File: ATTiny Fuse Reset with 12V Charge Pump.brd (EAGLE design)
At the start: 68.6 x 53.3 mm, 59 parts, among them IC1 74HC04D, Q1 BSS138, Q2 PMV65XP, Q3 BSS138, Q4 BSS138, Q5 BSS138, Q6 BSS138, Q7 BSS138, Q8 BSS130, SW4 SWITCH_SPDT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

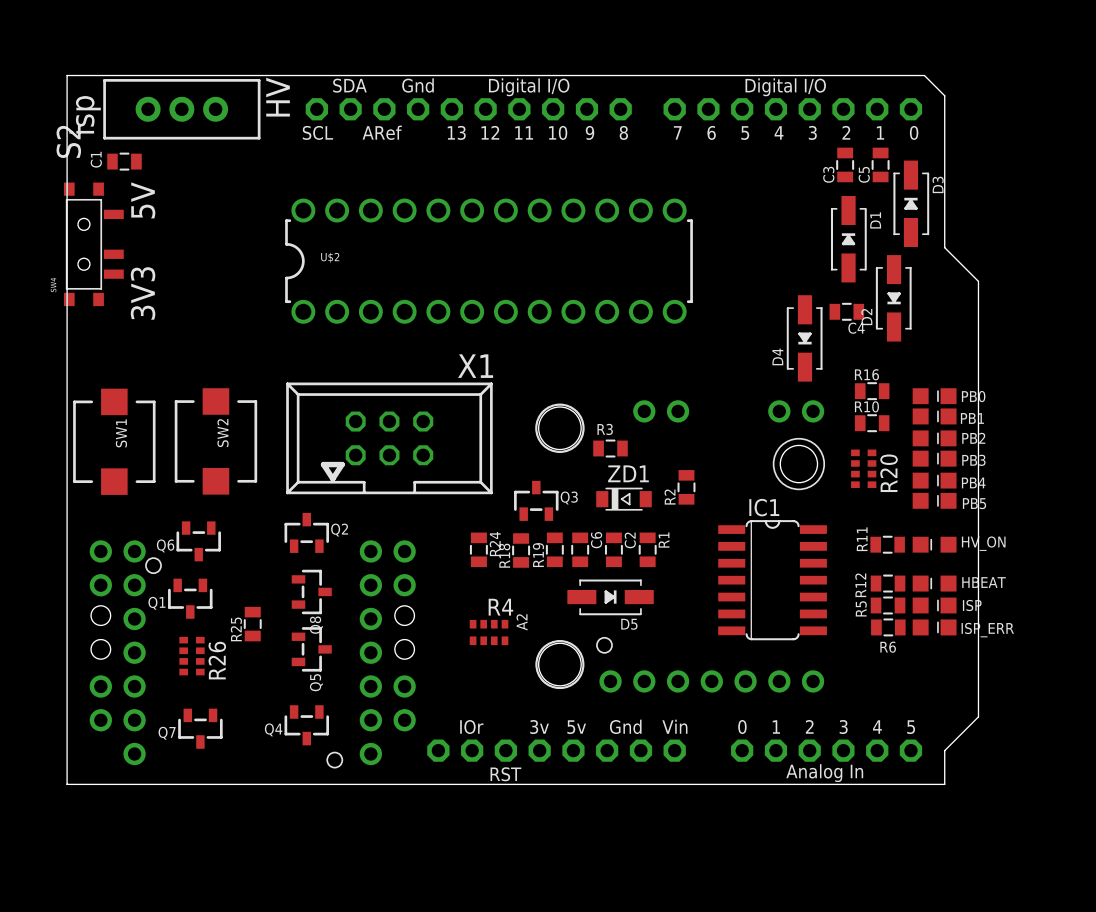
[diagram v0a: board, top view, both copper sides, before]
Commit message: removed pins from silkscreen on arduino device
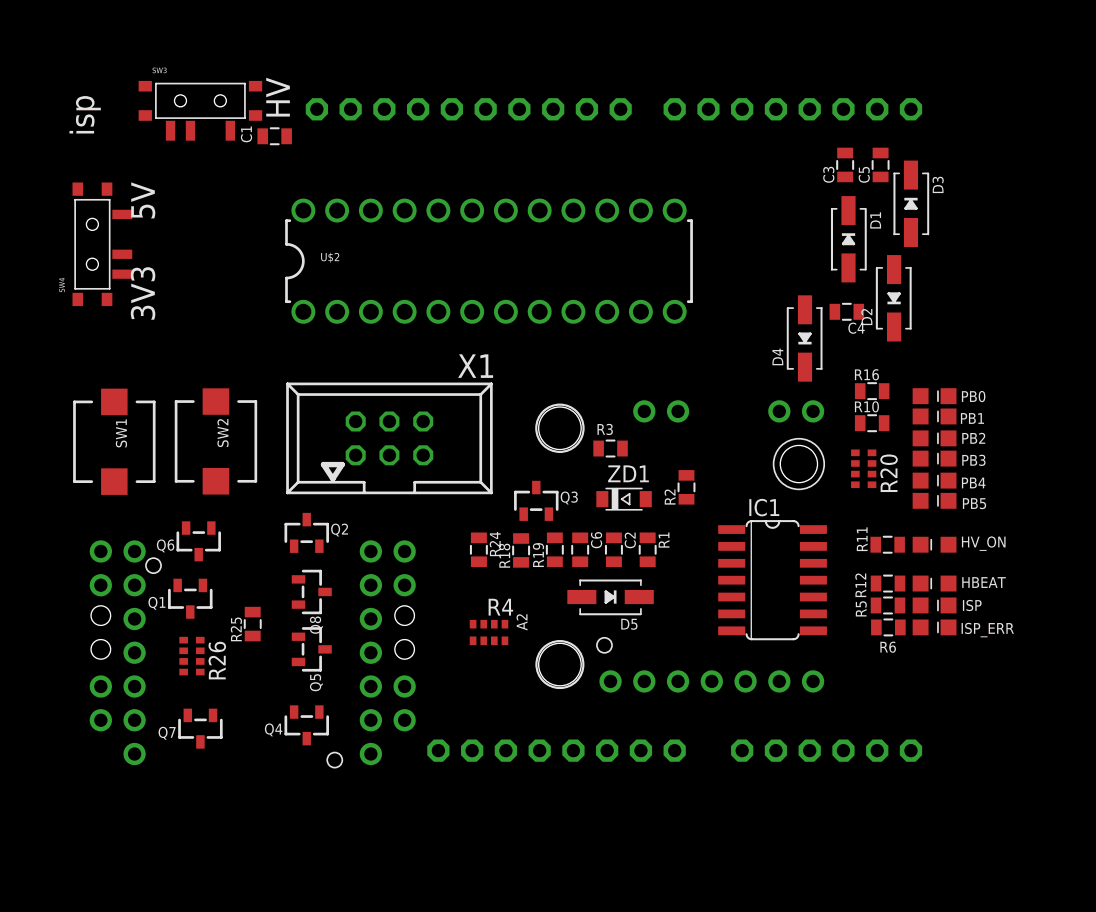
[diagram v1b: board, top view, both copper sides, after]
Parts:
- removed S2: (no value), SparkFun-Electromechanical:SWITCH-SPDT
- added SW3: SWITCH_SPDT, SparkFun-Electromechanical:KPS-1290
- U1: value ARDUINOR3 -> ARDUINOR3-BPLACE; device ATtami:ARDUINO_CLEAN -> ATtami:ARDUINOR3-BPLACE
- moved C1 11.5 mm to (15.6, 48.8)
- moved SW4 0.64 mm to (1.91, 40.6)
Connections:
- net GND: now also SW3.P; no longer S2.2
- net N$14: now also SW3.O; no longer S2.1
- net N$3: now also SW3.S; no longer S2.3
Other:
- board outline removed
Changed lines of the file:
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@@
 <layer number="23" name="tOrigins" color="15" fill="1" visible="yes" active="yes"/>
 <layer number="24" name="bOrigins" color="15" fill="1" visible="yes" active="yes"/>
-<layer number="25" name="tNames" color="7" fill="1" visible="yes" active="yes"/>
+<layer number="25" name="tNames" color="7" fill="1" visible="no" active="yes"/>
 <layer number="26" name="bNames" color="7" fill="1" visible="no" active="yes"/>
 <layer number="27" name="tValues" color="7" fill="1" visible="no" active="yes"/>
@@
 <attribute name="NAME" x="45.7835" y="20.955" size="0.8128" layer="25" rot="R90"/>
 </element>
-<element name="U1" library="ATtami" package="ARDUINO_CLEAN" value="ARDUINOR3" x="0" y="0"/>
+<element name="U1" library="ATtami" package="ARDUINOR3-BPLACE" value="ARDUINOR3-BPLACE" x="0" y="0"/>
 <element name="R11" library="ATtami" package="0805" value="220R" x="61.7474" y="18.034" smashed="yes" rot="R180">
 <attribute name="NAME" x="59.4233" y="19.431" size="0.8128" layer="25" rot="R270"/>
@@
 <attribute name="NAME" x="43.01" y="12.462" size="0.8128" layer="25" ratio="18" rot="R180"/>
 </element>
-<element name="C1" library="ATtami" package="0805" value="10uF" x="4.318" y="46.863" smashed="yes">
-<attribute name="NAME" x="2.6035" y="46.355" size="0.8128" layer="25" rot="R90"/>
-</element>
-<element name="SW4" library="SparkFun-Electromechanical" package="KPS-1290" value="SWITCH_SPDT" x="1.27" y="40.64" rot="R270"/>
+<element name="C1" library="ATtami" package="0805" value="10uF" x="15.621" y="48.768" smashed="yes">
+<attribute name="NAME" x="13.9065" y="48.26" size="0.8128" layer="25" rot="R90"/>
+</element>
+<element name="SW4" library="SparkFun-Electromechanical" package="KPS-1290" value="SWITCH_SPDT" x="1.905" y="40.64" rot="R270"/>
 <element name="ZD1" library="dp_devices" package="SOD-123" value="12V_zener" x="41.91" y="21.463" smashed="yes">
 <attribute name="NAME" x="40.64" y="22.733" size="1.27" layer="25" font="vector" ratio="10"/>
@@
 <element name="JP1" library="SparkFun-Connectors" package="1X02_PP_HOLES_ONLY" value="M02POGO_PIN_HOLES_ONLY" x="25.4" y="10.16" rot="R90"/>
 <element name="JP2" library="SparkFun-Connectors" package="1X02_PP_HOLES_ONLY" value="M02POGO_PIN_HOLES_ONLY" x="2.54" y="10.16" rot="R90"/>
-<element name="S2" library="SparkFun-Electromechanical" package="SWITCH-SPDT" value="" x="8.636" y="50.8" rot="R90">
-<attribute name="PROD_ID" value="SWCH-08261" x="8.636" y="50.8" size="1.778" layer="27" font="vector" ratio="15" rot="R90" display="off"/>
-</element>
 <element name="R4" library="SparkFun-Passives" package="0603-ARV" value="4k7" x="31.75" y="11.43" rot="R180"/>
 <element name="U$2" library="ATTiny Fuse Reset with 12V Charge Pump" package="DIL-24-ZIF" value="ZIFSOCKET-24" x="31.75" y="39.37"/>
+<element name="SW3" library="SparkFun-Electromechanical" package="KPS-1290" value="SWITCH_SPDT" x="10.033" y="51.435" rot="R180"/>
 </elements>
 <signals>
@@
 <contactref element="X1" pad="6"/>
 <contactref element="R25" pad="2"/>
-<contactref element="S2" pad="2"/>
-<contactref element="U1" pad="GND"/>
 <contactref element="U$2" pad="P$16"/>
 <contactref element="U$2" pad="P$18"/>
@@
 <contactref element="U$2" pad="P$17"/>
 <contactref element="U$2" pad="P$4"/>
+<contactref element="SW3" pad="P"/>
+<contactref element="U1" pad="GND"/>
 <wire x1="45.974" y1="28.067" x2="56.134" y2="28.067" width="0" layer="19" extent="1-1"/>
 <wire x1="46.609" y1="21.452" x2="45.974" y2="28.067" width="0" layer="19" extent="1-1"/>
@@
 <wire x1="26.416" y1="50.8" x2="30.48" y2="43.18" width="0" layer="19" extent="1-1"/>
 <wire x1="25.4" y1="7.366" x2="17.415" y2="13.528" width="0" layer="19" extent="1-1"/>
-<wire x1="8.636" y1="50.8" x2="26.416" y2="50.8" width="0" layer="19" extent="1-1"/>
+<wire x1="9.283" y1="49.185" x2="26.416" y2="50.8" width="0" layer="19" extent="1-1"/>
 </signal>
 <signal name="VIN">
@@
 <contactref element="R4" pad="6"/>
 <contactref element="R4" pad="5"/>
-<wire x1="30.55" y1="10.805" x2="3.52" y2="42.89" width="0" layer="19" extent="1-1"/>
+<wire x1="30.55" y1="10.805" x2="4.155" y2="42.89" width="0" layer="19" extent="1-1"/>
 <wire x1="31.35" y1="10.805" x2="30.55" y2="10.805" width="0" layer="19" extent="1-1"/>
 <wire x1="32.15" y1="10.805" x2="31.35" y2="10.805" width="0" layer="19" extent="1-1"/>
@@
 <contactref element="U1" pad="3V"/>
 <contactref element="SW4" pad="S"/>
-<wire x1="35.56" y1="2.54" x2="3.52" y2="38.39" width="0" layer="19" extent="1-1"/>
+<wire x1="35.56" y1="2.54" x2="4.155" y2="38.39" width="0" layer="19" extent="1-1"/>
 </signal>
 <signal name="N$13">
@@
 <signal name="N$14">
 <contactref element="C1" pad="1"/>
-<contactref element="S2" pad="1"/>
-<wire x1="3.418" y1="46.863" x2="6.096" y2="50.8" width="0" layer="19" extent="1-1"/>
+<contactref element="SW3" pad="O"/>
+<wire x1="12.283" y1="49.185" x2="14.721" y2="48.768" width="0" layer="19" extent="1-1"/>
 </signal>
 <signal name="N$33">
 <contactref element="C1" pad="2"/>
 <contactref element="U1" pad="RESET"/>
-<wire x1="33.02" y1="2.54" x2="5.218" y2="46.863" width="0" layer="19" extent="1-1"/>
+<wire x1="33.02" y1="2.54" x2="16.521" y2="48.768" width="0" layer="19" extent="1-1"/>
 </signal>
 <signal name="N$1">
 <contactref element="SW4" pad="P"/>
 <contactref element="Q2" pad="2"/>
-<wire x1="18.984" y1="17.923" x2="3.52" y2="39.89" width="0" layer="19" extent="1-1"/>
+<wire x1="18.984" y1="17.923" x2="4.155" y2="39.89" width="0" layer="19" extent="1-1"/>
 </signal>
 <signal name="N$9">
@@
 <wire x1="11.2014" y1="28.8064" x2="45.72" y2="50.8" width="0" layer="19" extent="1-1"/>
 </signal>
-<signal name="N$3">
-<contactref element="U1" pad="A0"/>
-<contactref element="S2" pad="3"/>
-<wire x1="50.8" y1="2.54" x2="11.176" y2="50.8" width="0" layer="19" extent="1-1"/>
-</signal>
 <signal name="N$23">
 <contactref element="PB2" pad="C"/>
@@
 <wire x1="9.271" y1="12.97" x2="59.319" y2="22.549" width="0" layer="19" extent="1-1"/>
 </signal>
+<signal name="N$3">
+<contactref element="U1" pad="A0"/>
+<contactref element="SW3" pad="S"/>
+<wire x1="50.8" y1="2.54" x2="7.783" y2="49.185" width="0" layer="19" extent="1-1"/>
+</signal>
 </signals>

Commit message: Captions added
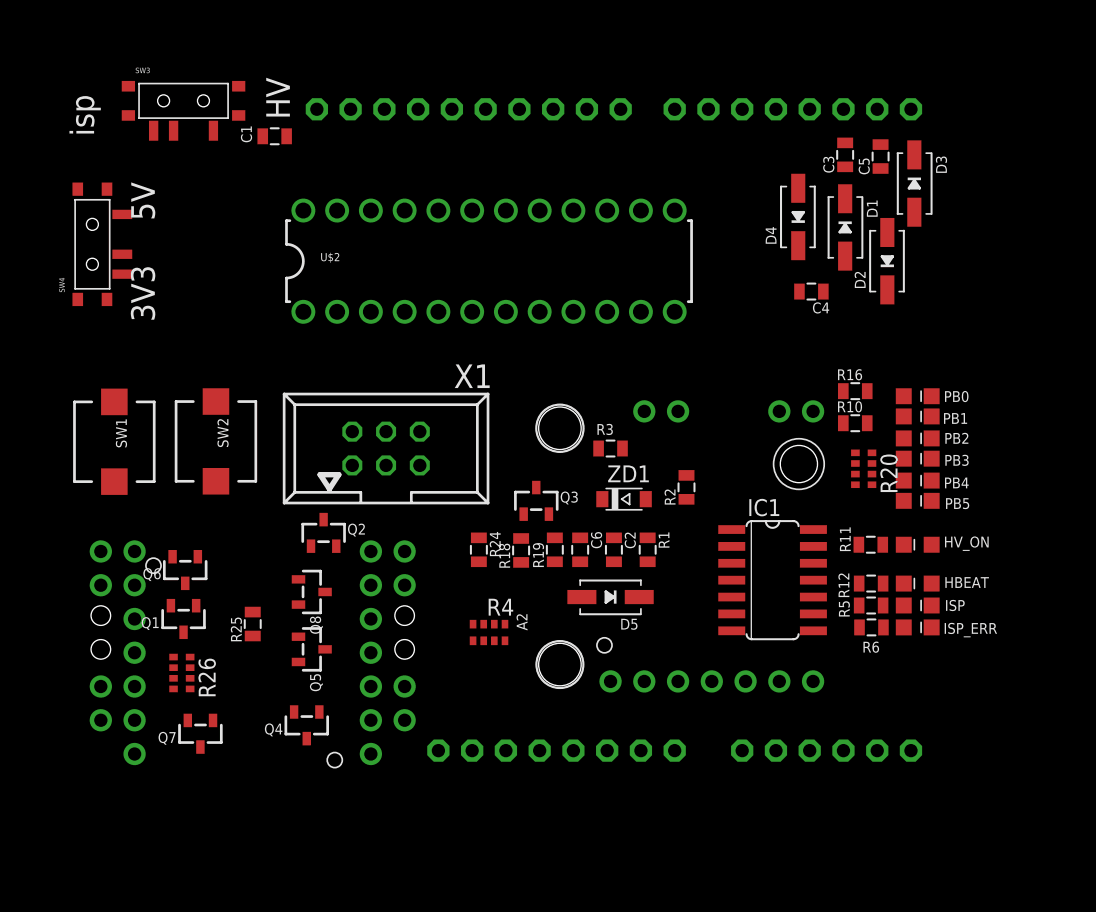
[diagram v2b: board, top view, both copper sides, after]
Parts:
- moved D4 9.16 mm to (55.0, 42.7)
- moved C4 3.07 mm to (56.0, 37.1)
- moved D2 2.84 mm to (61.7, 39.4)
- moved Q6 2.39 mm to (8.89, 16.1)
- moved Q1 1.61 mm to (8.76, 12.4)
- moved D3 1.55 mm to (63.8, 45.2)
- moved R26 1.48 mm to (8.64, 8.38)
- moved HBEAT 1.27 mm to (64.0, 15.1)
- moved HV_ON 1.27 mm to (64.0, 18.0)
- moved ISP 1.27 mm to (64.0, 13.5)
- moved ISP_ERR 1.27 mm to (64.0, 11.8)
- moved PB0 1.27 mm to (64.0, 29.2)
- moved PB1 1.27 mm to (64.0, 27.7)
- moved PB2 1.27 mm to (64.0, 26.0)
- moved PB3 1.27 mm to (64.0, 24.5)
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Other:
- board text added: "3.3V"
- board text added: "ATTami"
- board text added: "ATtiny"
- board text added: "ERR"
- board text added: "H.B."
- board text added: "ISP"
- board text added: "PB0"
- board text added: "PB1"
- board text added: "PB2"
- board text added: "PB3"
- board text added: "PB4"
- board text added: "PB5"
- board text added: "TAMI ATtiny HV / ISP Programmer"
- board text added: "load"
- board text added: "prog"
- board text added: "test"
- board text added: "|<--14 pin-->|"
- board text added: "|<8 pin>|"

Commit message: bit order and removed unsued layers
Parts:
- moved D3 8.08 mm to (58.0, 39.5)
- moved D1 7.59 mm to (51.3, 39.6), turned to 90 degrees
- moved R3 7.55 mm to (48.3, 23.6), turned to 0 degrees
- moved C4 7.07 mm to (53.8, 43.8)
- moved D4 6.98 mm to (61.2, 39.5)
- moved D2 6.86 mm to (54.9, 39.5)
- moved C6 5.46 mm to (44.1, 17.7)
- moved R1 4.57 mm to (39.1, 17.5)
- moved C3 3.87 mm to (57.0, 43.8), turned to 0 degrees
- moved C5 3.74 mm to (60.1, 43.7), turned to 180 degrees
- moved R2 2.18 mm to (44.8, 23.6), turned to 0 degrees
- moved ZD1 1.42 mm to (43.3, 21.2), turned to 180 degrees

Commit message: working on routng
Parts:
- moved C1 11.3 mm to (4.45, 47.1), turned to 270 degrees
- moved Q2 6.04 mm to (13.7, 16.6), turned to 180 degrees
- moved C3 4.58 mm to (59.6, 47.6)
- moved C4 4.58 mm to (56.4, 47.6)
- moved C5 4.58 mm to (62.6, 47.5)
- moved D2 3.59 mm to (57.4, 42.0)
- moved D1 3.59 mm to (53.8, 42.2)
- moved D3 3.59 mm to (60.6, 42.0)
- moved D4 3.59 mm to (63.8, 42.0)
- moved R2 2.54 mm to (42.3, 23.6)
- moved D5 2.18 mm to (39.1, 12.8)
- moved R26 2.09 mm to (10.7, 7.87)
- moved R4 1.80 mm to (30.5, 10.2)
- moved C2 1.55 mm to (41.4, 16.1)
- moved Q5 1.40 mm to (18.3, 8.76)
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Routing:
- net ATTINY_VCC: track 0.00 -> 151.3 mm, vias 0 -> 7
- net SII-MISO: track 0.00 -> 116.1 mm, vias 0 -> 5
- net SDO-SCK: track 0.00 -> 78.7 mm, vias 0 -> 5
- net N$9: track 0.00 -> 78.5 mm, vias 0 -> 1
- net HV/RESET: track 0.00 -> 78.3 mm, vias 0 -> 4
- net GND: track 0.00 -> 76.2 mm, vias 0 -> 1
- net SDI_MOSI: track 0.00 -> 74.9 mm, vias 0 -> 3
- net N$33: track 0.00 -> 65.8 mm, vias 0 -> 3
- net N$32: track 0.00 -> 64.7 mm, vias 0 -> 4
- net VCC_OFF: track 0.00 -> 63.5 mm, vias 0 -> 3
- net VCC: track 0.00 -> 63.0 mm
- net SCI: track 0.00 -> 61.8 mm, vias 0 -> 5
- net N$8: track 0.00 -> 61.3 mm, vias 0 -> 2
- net N$16: track 0.00 -> 57.9 mm, vias 0 -> 2
- net N$37: track 0.00 -> 56.5 mm, vias 0 -> 2
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- added copper zone on layer 1, net GND

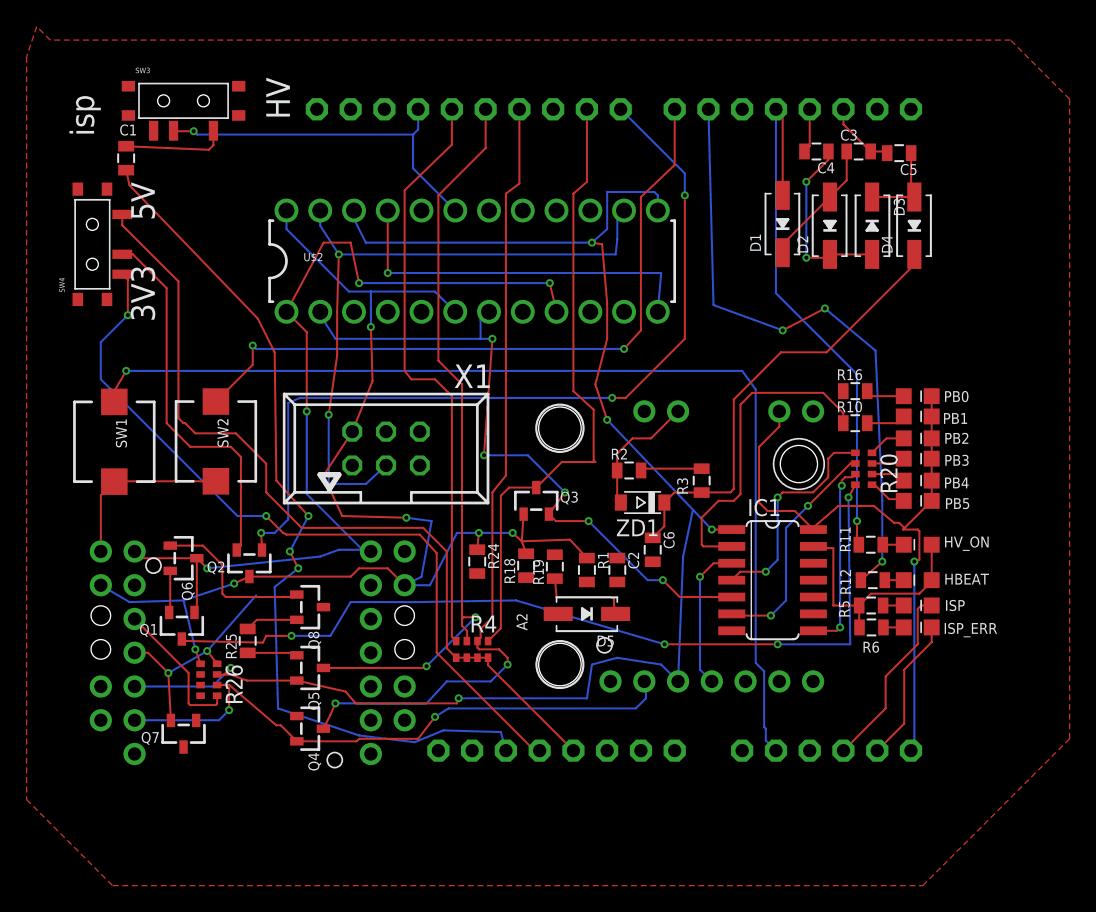
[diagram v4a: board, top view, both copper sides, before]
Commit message: more routing, now switching for topoR
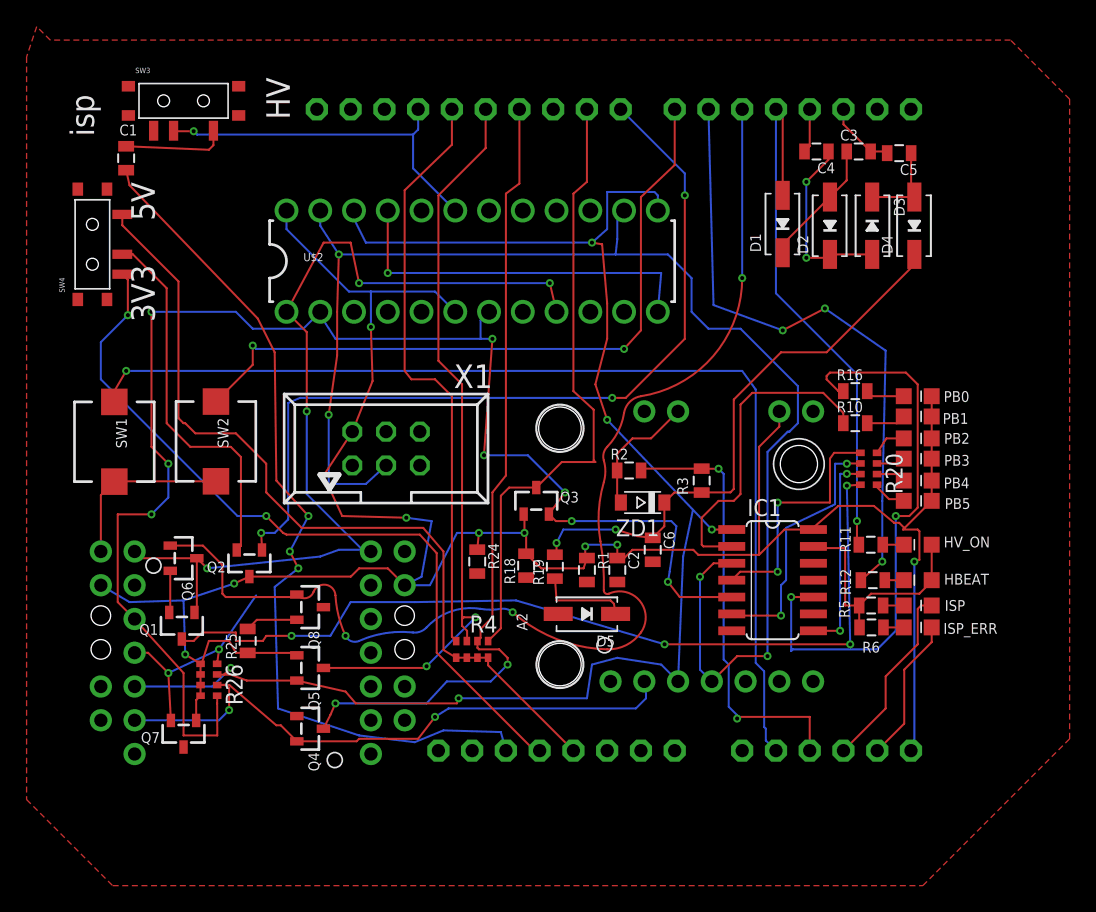
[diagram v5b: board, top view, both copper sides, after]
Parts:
- moved R20 0.38 mm to (60.3, 23.7)
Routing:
- net HV_OFF(RESET): track 12.5 -> 86.2 mm, vias 0 -> 3
- net SCI: track 61.8 -> 110.8 mm, vias 5 -> 8
- net SDO-SCK: track 78.7 -> 124.4 mm, vias 5 -> 6
- net N$13: track 0.00 -> 43.4 mm, vias 0 -> 2
- net ATTINY_VCC: track 151.3 -> 181.2 mm, vias 7 -> 9
- net HV_SENSE: track 4.62 -> 33.3 mm, vias 0 -> 2
- net 11.5V: track 34.0 -> 42.8 mm, vias 0 -> 2
- net N$26: track 17.3 -> 19.6 mm
- net N$24: track 16.8 -> 18.7 mm
- net N$32: track 64.7 -> 66.3 mm
- net N$28: track 14.4 -> 15.4 mm
- net N$19: track 46.8 -> 47.4 mm
